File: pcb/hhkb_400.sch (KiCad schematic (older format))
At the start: 152 parts, among them J1 USB_mini_micro_B, SW1 SW_PUSH, U1 ATMEGA32U4, X1 XTAL_GND

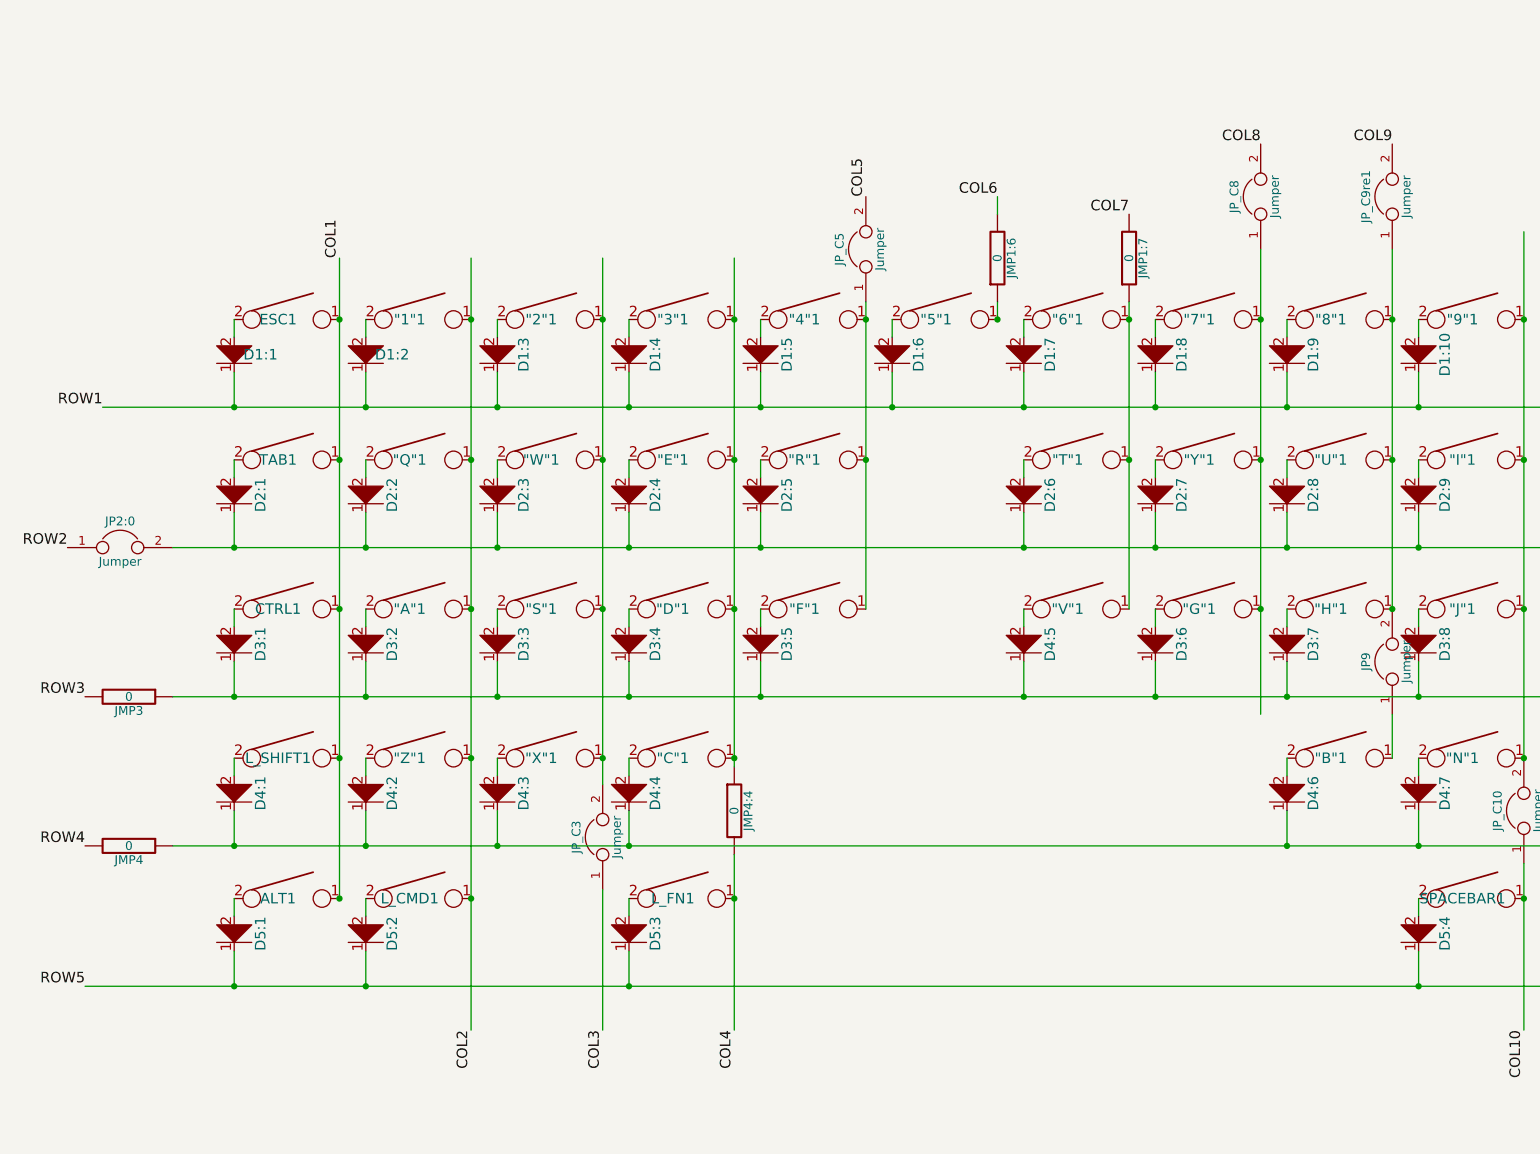
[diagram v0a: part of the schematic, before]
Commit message: use jumper to represent jumper, rather than 0ohm resister
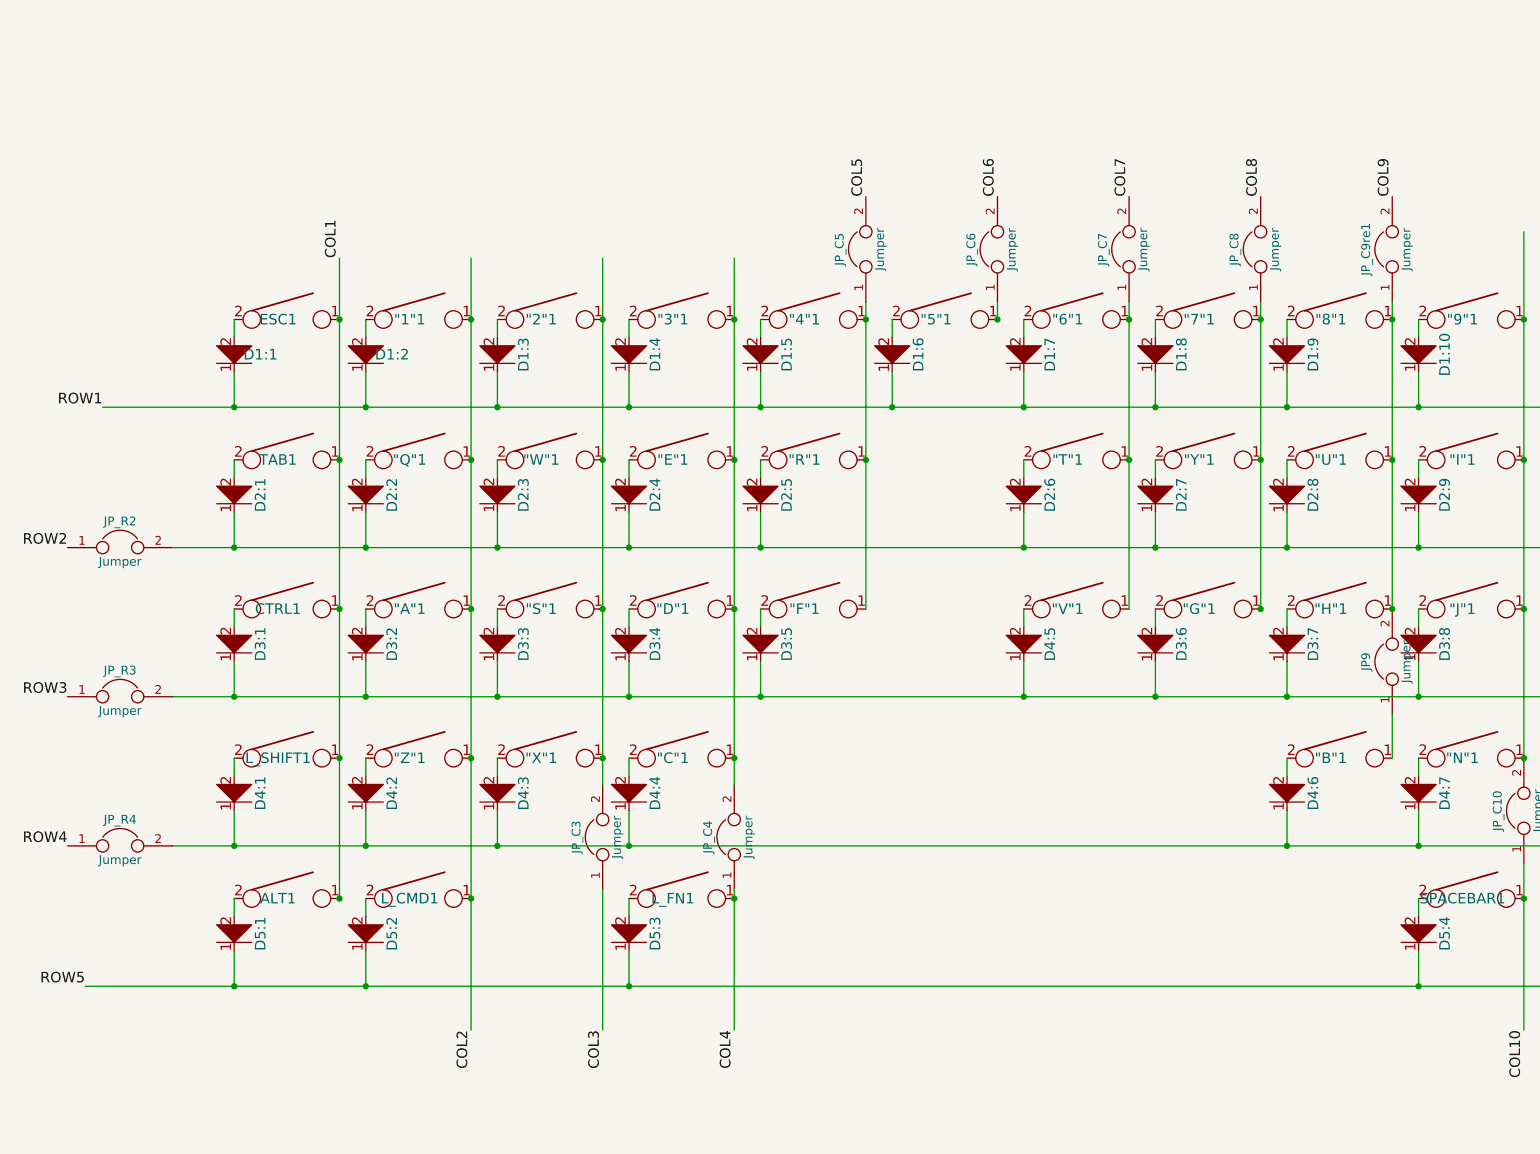
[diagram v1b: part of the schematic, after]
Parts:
- removed JMP1:6, JMP1:7, JMP3, JMP4, JMP4:4: 0, Resistors_SMD:R_1206_HandSoldering, symbol R
- added JP_C4, JP_C6, JP_C7, JP_R3, JP_R4: Jumper, Resistors_SMD:R_1206_HandSoldering, symbol Jumper
- renumbered JP2:0 to JP_R2
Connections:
- net COL4: now also JP_C4.1
- net COL6: now also JP_C6.2
- net COL7: now also JP_C7.2
- net ROW3: now also JP_R3.1
- net ROW4: now also JP_R4.1
- net at "5"1.1: now also JP_C6.1
- net at "6"1.1, "T"1.1, "V"1.1: now also JP_C7.1
- net at "3"1.1, "C"1.1, "D"1.1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: now also JP_C4.2
- net at D3:1.1, D3:10.1, D3:11.1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: now also JP_R3.2
- net at D4:1.1, D4:10.1, D4:11.1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: now also JP_R4.2
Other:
- moved on the sheet: JP_C8, JP_C9re1
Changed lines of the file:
@@
-$EndComp
-$Comp
-L KEYSW L_FN1
-U 1 1 58ABBCEE
-P 5250 5150
-F 0 "L_FN1" H 5200 5150 60  0000 C CNN
-F 1 "KEYSW" H 5250 5050 60  0001 C CNN
-F 2 "TheKeebrary:MX_Plate_150H" H 5250 5150 60  0001 C CNN
-F 3 "" H 5250 5150 60  0000 C CNN
-	1    5250 5150
-	1    0    0    -1
 $EndComp
 $Comp
@@
 Text Label 1950 2350 2    60   ~ 0
 ROW1
-Text Label 1850 4000 2    60   ~ 0
+Text Label 1750 4000 2    60   ~ 0
 ROW3
-Text Label 1850 4850 2    60   ~ 0
+Text Label 1750 4850 2    60   ~ 0
 ROW4
 Text Label 1850 5650 2    60   ~ 0
@@
 Text Label 3300 1500 1    60   ~ 0
 COL1
-Text Label 7050 1150 2    60   ~ 0
+Text Label 7050 1150 1    60   ~ 0
 COL6
-Text Label 7800 1250 2    60   ~ 0
+Text Label 7800 1150 1    60   ~ 0
 COL7
-Text Label 8550 850  2    60   ~ 0
+Text Label 8550 1150 1    60   ~ 0
 COL8
 Text Label 10050 5900 3    60   ~ 0
@@
 Text Label 7850 8950 0    60   ~ 0
 COL11
-$Comp
-L R JMP4
-U 1 1 58AEBAD4
-P 2100 4850
-F 0 "JMP4" V 2180 4850 50  0000 C CNN
-F 1 "0" V 2100 4850 50  0000 C CNN
-F 2 "Resistors_SMD:R_1206_HandSoldering" H 2100 4850 60  0001 C CNN
-F 3 "" H 2100 4850 60  0000 C CNN
-	1    2100 4850
-	0    1    1    0
-$EndComp
-$Comp
-L R JMP3
-U 1 1 58AEEC71
-P 2100 4000
-F 0 "JMP3" V 2180 4000 50  0000 C CNN
-F 1 "0" V 2100 4000 50  0000 C CNN
-F 2 "Resistors_SMD:R_1206_HandSoldering" H 2100 4000 60  0001 C CNN
-F 3 "" H 2100 4000 60  0000 C CNN
-	1    2100 4000
-	0    1    1    0
-$EndComp
 Text Label 5600 9850 2    60   ~ 0
 ROW3
@@
 ROW2
 $Comp
-L Jumper JP2:0
+L Jumper JP_R2
 U 1 1 58B1775C
 P 2050 3150
-F 0 "JP2:0" H 2050 3300 50  0000 C CNN
+F 0 "JP_R2" H 2050 3300 50  0000 C CNN
 F 1 "Jumper" H 2050 3070 50  0000 C CNN
 F 2 "Resistors_SMD:R_1206_HandSoldering" H 2050 3150 50  0001 C CNN
@@
 Text Label 7850 9350 0    60   ~ 0
 ROW2
-Text Label 9300 850  2    60   ~ 0
+Text Label 9300 1150 1    60   ~ 0
 COL9
 Text Label 7850 9550 0    60   ~ 0
@@
 L Jumper JP_C9re1
 U 1 1 58B261AB
-P 9300 1150
-F 0 "JP_C9re1" H 9300 1300 50  0000 C CNN
-F 1 "Jumper" H 9300 1070 50  0000 C CNN
-F 2 "Resistors_SMD:R_1206_HandSoldering" H 9300 1150 50  0001 C CNN
-F 3 "" H 9300 1150 50  0000 C CNN
-	1    9300 1150
+P 9300 1450
+F 0 "JP_C9re1" H 9300 1600 50  0000 C CNN
+F 1 "Jumper" H 9300 1370 50  0000 C CNN
+F 2 "Resistors_SMD:R_1206_HandSoldering" H 9300 1450 50  0001 C CNN
+F 3 "" H 9300 1450 50  0000 C CNN
+	1    9300 1450
 	0    -1   -1   0
 $EndComp
@@
 L Jumper JP_C8
 U 1 1 58B2A275
-P 8550 1150
-F 0 "JP_C8" H 8550 1300 50  0000 C CNN
-F 1 "Jumper" H 8550 1070 50  0000 C CNN
-F 2 "Resistors_SMD:R_1206_HandSoldering" H 8550 1150 50  0001 C CNN
-F 3 "" H 8550 1150 50  0000 C CNN
-	1    8550 1150
+P 8550 1450
+F 0 "JP_C8" H 8550 1600 50  0000 C CNN
+F 1 "Jumper" H 8550 1370 50  0000 C CNN
+F 2 "Resistors_SMD:R_1206_HandSoldering" H 8550 1450 50  0001 C CNN
+F 3 "" H 8550 1450 50  0000 C CNN
+	1    8550 1450
 	0    -1   -1   0
-$EndComp
-$Comp
-L R JMP1:6
-U 1 1 58AF5E65
-P 7050 1500
-F 0 "JMP1:6" V 7130 1500 50  0000 C CNN
-F 1 "0" V 7050 1500 50  0000 C CNN
-F 2 "Resistors_SMD:R_1206_HandSoldering" H 7050 1500 60  0001 C CNN
-F 3 "" H 7050 1500 60  0000 C CNN
-	1    7050 1500
-	1    0    0    1
-$EndComp
-$Comp
-L R JMP1:7
-U 1 1 58B0E3FF
-P 7800 1500
-F 0 "JMP1:7" V 7880 1500 50  0000 C CNN
-F 1 "0" V 7800 1500 50  0000 C CNN
-F 2 "Resistors_SMD:R_1206_HandSoldering" H 7800 1500 60  0001 C CNN
-F 3 "" H 7800 1500 60  0000 C CNN
-	1    7800 1500
-	1    0    0    1
 $EndComp
 $Comp
@@
 	1    9300 3800
 	0    -1   -1   0
-$EndComp
-$Comp
-L R JMP4:4
-U 1 1 58B58829
-P 5550 4650
-F 0 "JMP4:4" V 5630 4650 50  0000 C CNN
-F 1 "0" V 5550 4650 50  0000 C CNN
-F 2 "Resistors_SMD:R_1206_HandSoldering" H 5550 4650 60  0001 C CNN
-F 3 "" H 5550 4650 60  0000 C CNN
-	1    5550 4650
-	1    0    0    -1
 $EndComp
 $Comp
@@
 Connection ~ 4800 1850
 Connection ~ 4050 1850
-Wire Wire Line
-	8550 1450 8550 4100
 Connection ~ 10050 4350
 Connection ~ 10050 2650
@@
 Connection ~ 4950 3150
 Connection ~ 5700 3150
-Wire Wire Line
-	5550 4900 5550 5900
 Connection ~ 5550 5150
 Wire Wire Line
-	5550 1500 5550 4400
+	5550 1500 5550 4500
 Wire Wire Line
 	4800 1500 4800 4500
@@
 Connection ~ 4050 5150
 Connection ~ 4800 4350
-Wire Wire Line
-	7050 1150 7050 1250
 Wire Wire Line
 	7050 1750 7050 1850
@@
 	4800 5100 4800 5900
 Wire Wire Line
-	9300 1450 9300 3500
-Wire Wire Line
 	3300 1500 3300 5150
 $Comp
@@
 Wire Wire Line
 	6300 1750 6300 3500
+$Comp
+L Jumper JP_C6
+U 1 1 58ADE8EE
+P 7050 1450
+F 0 "JP_C6" H 7050 1600 50  0000 C CNN
+F 1 "Jumper" H 7050 1370 50  0000 C CNN
+F 2 "Resistors_SMD:R_1206_HandSoldering" H 7050 1450 50  0001 C CNN
+F 3 "" H 7050 1450 50  0000 C CNN
+	1    7050 1450
+	0    -1   -1   0
+$EndComp
+$Comp
+L Jumper JP_C7
+U 1 1 58ADF16F
+P 7800 1450
+F 0 "JP_C7" H 7800 1600 50  0000 C CNN
+F 1 "Jumper" H 7800 1370 50  0000 C CNN
+F 2 "Resistors_SMD:R_1206_HandSoldering" H 7800 1450 50  0001 C CNN
+F 3 "" H 7800 1450 50  0000 C CNN
+	1    7800 1450
+	0    -1   -1   0
+$EndComp
+Wire Wire Line
+	9300 1750 9300 3500
+Wire Wire Line
+	8550 1750 8550 3500
+$Comp
+L Jumper JP_C4
+U 1 1 58AE3471
+P 5550 4800
+F 0 "JP_C4" H 5550 4950 50  0000 C CNN
+F 1 "Jumper" H 5550 4720 50  0000 C CNN
+F 2 "Resistors_SMD:R_1206_HandSoldering" H 5550 4800 50  0001 C CNN
+F 3 "" H 5550 4800 50  0000 C CNN
+	1    5550 4800
+	0    -1   -1   0
+$EndComp
+$Comp
+L KEYSW L_FN1
+U 1 1 58ABBCEE
+P 5250 5150
+F 0 "L_FN1" H 5200 5150 60  0000 C CNN
+F 1 "KEYSW" H 5250 5050 60  0001 C CNN
+F 2 "TheKeebrary:MX_Plate_150H" H 5250 5150 60  0001 C CNN
+F 3 "" H 5250 5150 60  0000 C CNN
+	1    5250 5150
+	1    0    0    -1
+$EndComp
+Wire Wire Line
+	5550 5100 5550 5900
+$Comp
+L Jumper JP_R3
+U 1 1 58AE5187
+P 2050 4000
+F 0 "JP_R3" H 2050 4150 50  0000 C CNN
+F 1 "Jumper" H 2050 3920 50  0000 C CNN
+F 2 "Resistors_SMD:R_1206_HandSoldering" H 2050 4000 50  0001 C CNN
+F 3 "" H 2050 4000 50  0000 C CNN
+	1    2050 4000
+	1    0    0    -1
+$EndComp
+$Comp
+L Jumper JP_R4
+U 1 1 58AE60FD
+P 2050 4850
+F 0 "JP_R4" H 2050 5000 50  0000 C CNN
+F 1 "Jumper" H 2050 4770 50  0000 C CNN
+F 2 "Resistors_SMD:R_1206_HandSoldering" H 2050 4850 50  0001 C CNN
+F 3 "" H 2050 4850 50  0000 C CNN
+	1    2050 4850
+	1    0    0    -1
+$EndComp
 $EndSCHEMATC

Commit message: update
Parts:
- removed D5:3: D, Diodes_SMD:D_SOD-123, symbol D
- removed L_FN1: KEYSW, TheKeebrary:MX_Plate_150H, symbol KEYSW
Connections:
- net COL13: now also R_CMD1.2
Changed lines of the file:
@@
-$EndComp
-$Comp
-L D D5:3
-U 1 1 58ACC58C
-P 4950 5400
-F 0 "D5:3" V 4800 5350 60  0000 C CNN
-F 1 "D" V 5100 5350 60  0001 C CNN
-F 2 "Diodes_SMD:D_SOD-123" H 4950 5400 60  0001 C CNN
-F 3 "" H 4950 5400 60  0000 C CNN
-	1    4950 5400
-	-1   0    0    1
 $EndComp
 $Comp
@@
 Connection ~ 2700 5650
 Connection ~ 3450 5650
-Connection ~ 4950 5650
 Connection ~ 9450 5650
 Connection ~ 9450 4000
@@
 	4950 4350 4950 4450
 Wire Wire Line
-	4950 5150 4950 5250
-Wire Wire Line
 	4200 4350 4200 4450
 Wire Wire Line
@@
 Wire Wire Line
 	9450 5450 9450 5650
-Wire Wire Line
-	4950 5450 4950 5650
 Wire Wire Line
 	3450 5450 3450 5650
@@
 Connection ~ 4950 3150
 Connection ~ 5700 3150
-Connection ~ 5550 5150
 Wire Wire Line
 	5550 1500 5550 4500
@@
 Connection ~ 13000 1850
 Wire Wire Line
-	12250 1350 12250 4350
+	12250 1350 12250 5150
 Connection ~ 12250 1850
 Connection ~ 12250 2650
@@
 	0    -1   -1   0
 $EndComp
-$Comp
-L KEYSW L_FN1
-U 1 1 58ABBCEE
-P 5250 5150
-F 0 "L_FN1" H 5200 5150 60  0000 C CNN
-F 1 "KEYSW" H 5250 5050 60  0001 C CNN
-F 2 "TheKeebrary:MX_Plate_150H" H 5250 5150 60  0001 C CNN
-F 3 "" H 5250 5150 60  0000 C CNN
-	1    5250 5150
-	1    0    0    -1
-$EndComp
 Wire Wire Line
 	5550 5100 5550 5900
@@
 	1    0    0    -1
 $EndComp
+Connection ~ 12250 4350
 $EndSCHEMATC
